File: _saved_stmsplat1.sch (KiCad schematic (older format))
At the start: 74 parts, among them CN1 Conn_01x16_Male, CN2 Conn_01x30_Male, CN3 Conn_01x20_Male, CN4 Conn_01x34_Male, J1 Conn_Coaxial, J2 Conn_01x04_Male, J3 Conn_01x04_Male, U1 NUCLEO144-F746ZG, U10 MPL315A2, U11 XBee3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

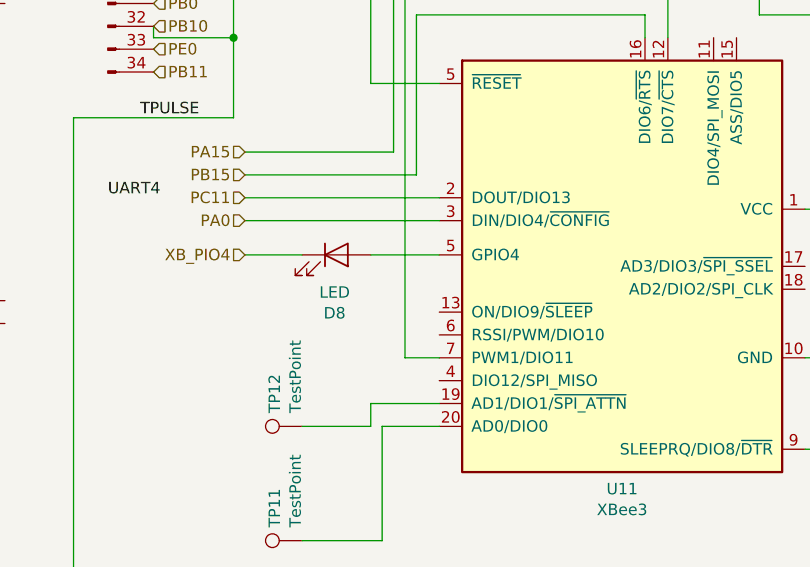
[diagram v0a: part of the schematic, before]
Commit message: Fix Xbee extra symbol pin, change via sizes on power
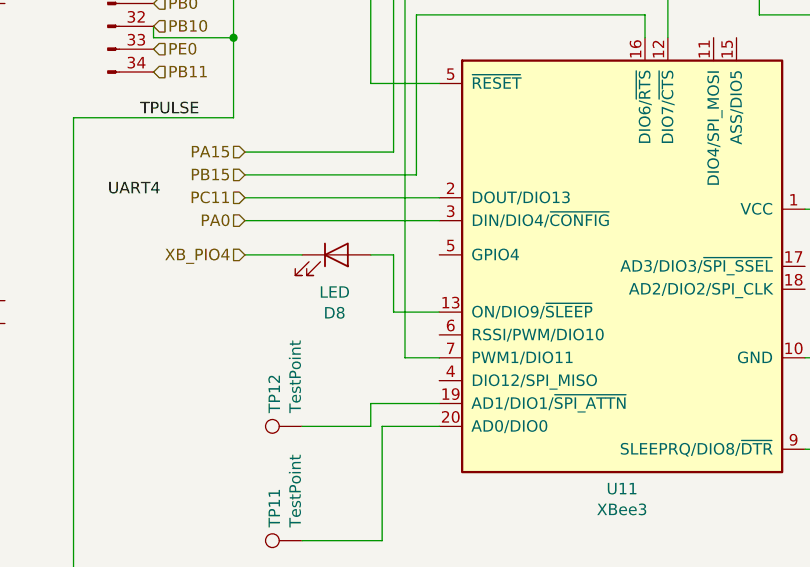
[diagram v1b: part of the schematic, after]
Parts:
- removed U11: XBee3, spatboard:XBEE-22MM-TH, symbol stmsplat1-rescue:XBee3-splatlib
- added U11: XBee3, spatboard:XBEE-22MM-TH, symbol splatlib:XBee3
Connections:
- net GND: now also U11.10 (GND)
- net P3V3: now also U11.1 (VCC)
- net PA0: now also U11.3 (DIN/DIO4/~CONFIG)
- net PA15: now also U11.12 (DIO7/~CTS)
- net PB15: now also U11.16 (DIO6/~RTS)
- net PC11: now also U11.2 (DOUT/DIO13)
- net PE10: now also U11.9 (SLEEPRQ/DIO8/~DTR)
- net PE15: now also U11.5 (~RESET)
- net at TP12.1: now also U11.19 (AD1/DIO1/~SPI_ATTN)
- net at TP11.1: now also U11.20 (AD0/DIO0)
- net at D8.2 (A): now also U11.13 (ON/DIO9/~SLEEP)
- net at U8.9: now also U11.7 (PWM1/DIO11)
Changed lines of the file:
@@
 Wire Wire Line
 	8350 8100 8350 8000
-$Comp
-L stmsplat1-rescue:XBee3-splatlib U11
-U 1 1 5BFA172B
-P 7350 7600
-F 0 "U11" H 7350 6626 50  0000 C CNN
-F 1 "XBee3" H 7350 6535 50  0000 C CNN
-F 2 "spatboard:XBEE-22MM-TH" H 7500 7700 50  0001 C CNN
-F 3 "http://www.ti.com/lit/gpn/cc2520" H 7350 7350 50  0001 C CNN
-	1    7350 7600
-	1    0    0    -1
-$EndComp
 Wire Wire Line
 	7550 6600 7550 6400
@@
 Wire Wire Line
 	5100 10150 5100 9550
-Wire Wire Line
-	6550 7550 6250 7550
+$Comp
+L splatlib:XBee3 U11
+U 1 1 5C4E2737
+P 7350 7600
+F 0 "U11" H 7350 6626 50  0000 C CNN
+F 1 "XBee3" H 7350 6535 50  0000 C CNN
+F 2 "spatboard:XBEE-22MM-TH" H 7500 7700 50  0001 C CNN
+F 3 "http://www.ti.com/lit/gpn/cc2520" H 7350 7350 50  0001 C CNN
+	1    7350 7600
+	1    0    0    -1
+$EndComp
+Wire Wire Line
+	6550 7800 6350 7800
+Wire Wire Line
+	6350 7800 6350 7550
+Wire Wire Line
+	6350 7550 6250 7550
 $EndSCHEMATC
